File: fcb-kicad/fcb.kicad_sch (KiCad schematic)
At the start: 50 parts, among them J1 Conn_ESC_4in1, J2 SWD, SW1 SW_Push, SW2 SW_SPDT, U1 TPS5430DDA, U2 AMS1117-3.3, U5 STM32F411CEUx, Y1 16 MHz

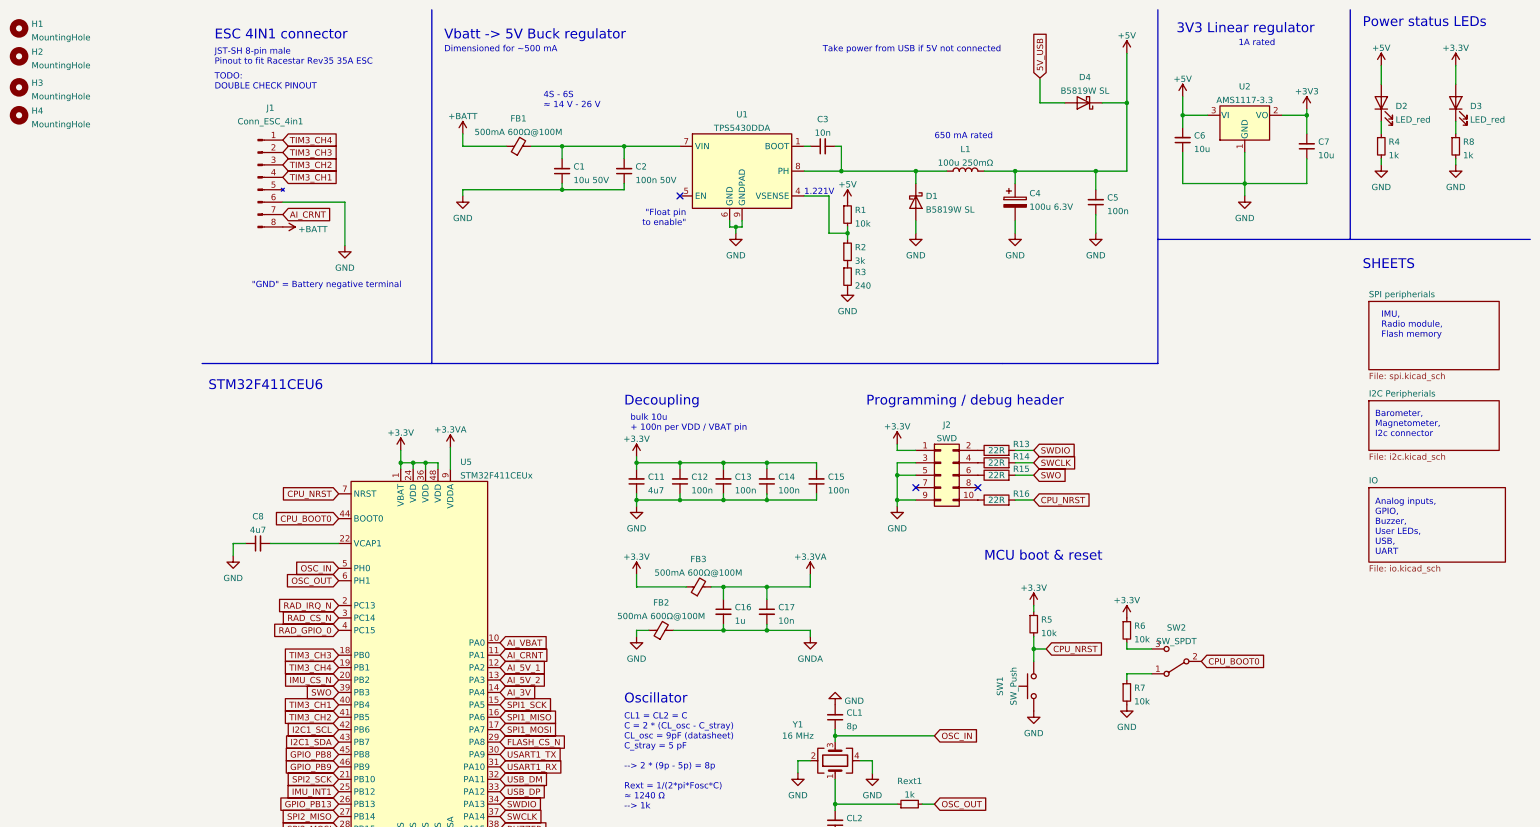
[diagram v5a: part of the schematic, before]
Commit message: buzzer footprint
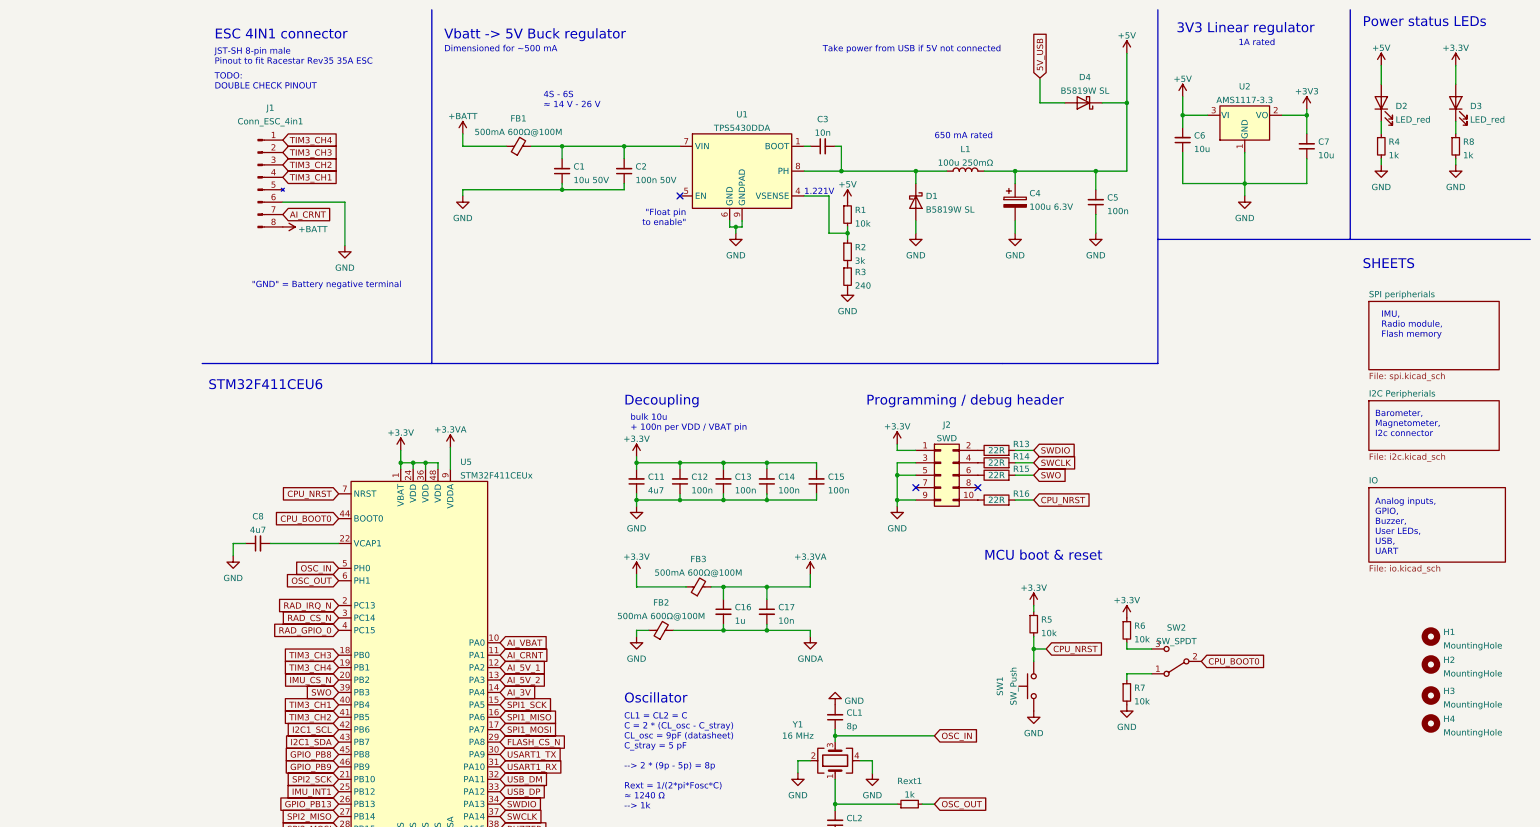
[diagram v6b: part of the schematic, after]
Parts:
- H1, H2, H3, H4: footprint MountingHole:MountingHole_3.2mm_M3 -> MountingHole:MountingHole_3.2mm_M3_DIN965_Pad
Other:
- moved on the sheet: H1, H2, H3, H4
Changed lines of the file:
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@@
     (pin "2")
   )
-  (symbol (lib_id "Mechanical:MountingHole") (at -24.765 34.29 0) (unit 1)
-    (in_bom yes) (on_board yes) (fields_autoplaced)
-    (property "Reference" "H4" (id 0) (at -22.225 33.3815 0)
-      (effects (font (size 1.27 1.27)) (justify left))
-    )
-    (property "Value" "MountingHole" (id 1) (at -22.225 36.1566 0)
-      (effects (font (size 1.27 1.27)) (justify left))
-    )
-    (property "Footprint" "MountingHole:MountingHole_3.2mm_M3" (id 2) (at -24.765 34.29 0)
-      (effects (font (size 1.27 1.27)) hide)
-    )
-    (property "Datasheet" "~" (id 3) (at -24.765 34.29 0)
+  (symbol (lib_id "Mechanical:MountingHole") (at 264.16 158.75 0) (unit 1)
+    (in_bom yes) (on_board yes) (fields_autoplaced)
+    (property "Reference" "H4" (id 0) (at 266.7 157.8415 0)
+      (effects (font (size 1.27 1.27)) (justify left))
+    )
+    (property "Value" "MountingHole" (id 1) (at 266.7 160.6166 0)
+      (effects (font (size 1.27 1.27)) (justify left))
+    )
+    (property "Footprint" "MountingHole:MountingHole_3.2mm_M3_DIN965_Pad" (id 2) (at 264.16 158.75 0)
+      (effects (font (size 1.27 1.27)) hide)
+    )
+    (property "Datasheet" "~" (id 3) (at 264.16 158.75 0)
       (effects (font (size 1.27 1.27)) hide)
     )
@@
     (pin "2")
   )
-  (symbol (lib_id "Mechanical:MountingHole") (at -24.765 16.51 0) (unit 1)
-    (in_bom yes) (on_board yes) (fields_autoplaced)
-    (property "Reference" "H1" (id 0) (at -22.225 15.6015 0)
-      (effects (font (size 1.27 1.27)) (justify left))
-    )
-    (property "Value" "MountingHole" (id 1) (at -22.225 18.3766 0)
-      (effects (font (size 1.27 1.27)) (justify left))
-    )
-    (property "Footprint" "MountingHole:MountingHole_3.2mm_M3" (id 2) (at -24.765 16.51 0)
-      (effects (font (size 1.27 1.27)) hide)
-    )
-    (property "Datasheet" "~" (id 3) (at -24.765 16.51 0)
+  (symbol (lib_id "Mechanical:MountingHole") (at 264.16 140.97 0) (unit 1)
+    (in_bom yes) (on_board yes) (fields_autoplaced)
+    (property "Reference" "H1" (id 0) (at 266.7 140.0615 0)
+      (effects (font (size 1.27 1.27)) (justify left))
+    )
+    (property "Value" "MountingHole" (id 1) (at 266.7 142.8366 0)
+      (effects (font (size 1.27 1.27)) (justify left))
+    )
+    (property "Footprint" "MountingHole:MountingHole_3.2mm_M3_DIN965_Pad" (id 2) (at 264.16 140.97 0)
+      (effects (font (size 1.27 1.27)) hide)
+    )
+    (property "Datasheet" "~" (id 3) (at 264.16 140.97 0)
       (effects (font (size 1.27 1.27)) hide)
     )
@@
     (pin "1")
   )
-  (symbol (lib_id "Mechanical:MountingHole") (at -24.765 28.575 0) (unit 1)
-    (in_bom yes) (on_board yes) (fields_autoplaced)
-    (property "Reference" "H3" (id 0) (at -22.225 27.6665 0)
-      (effects (font (size 1.27 1.27)) (justify left))
-    )
-    (property "Value" "MountingHole" (id 1) (at -22.225 30.4416 0)
-      (effects (font (size 1.27 1.27)) (justify left))
-    )
-    (property "Footprint" "MountingHole:MountingHole_3.2mm_M3" (id 2) (at -24.765 28.575 0)
-      (effects (font (size 1.27 1.27)) hide)
-    )
-    (property "Datasheet" "~" (id 3) (at -24.765 28.575 0)
+  (symbol (lib_id "Mechanical:MountingHole") (at 264.16 153.035 0) (unit 1)
+    (in_bom yes) (on_board yes) (fields_autoplaced)
+    (property "Reference" "H3" (id 0) (at 266.7 152.1265 0)
+      (effects (font (size 1.27 1.27)) (justify left))
+    )
+    (property "Value" "MountingHole" (id 1) (at 266.7 154.9016 0)
+      (effects (font (size 1.27 1.27)) (justify left))
+    )
+    (property "Footprint" "MountingHole:MountingHole_3.2mm_M3_DIN965_Pad" (id 2) (at 264.16 153.035 0)
+      (effects (font (size 1.27 1.27)) hide)
+    )
+    (property "Datasheet" "~" (id 3) (at 264.16 153.035 0)
       (effects (font (size 1.27 1.27)) hide)
     )
@@
     (pin "1")
   )
-  (symbol (lib_id "Mechanical:MountingHole") (at -24.765 22.225 0) (unit 1)
-    (in_bom yes) (on_board yes) (fields_autoplaced)
-    (property "Reference" "H2" (id 0) (at -22.225 21.3165 0)
-      (effects (font (size 1.27 1.27)) (justify left))
-    )
-    (property "Value" "MountingHole" (id 1) (at -22.225 24.0916 0)
-      (effects (font (size 1.27 1.27)) (justify left))
-    )
-    (property "Footprint" "MountingHole:MountingHole_3.2mm_M3" (id 2) (at -24.765 22.225 0)
-      (effects (font (size 1.27 1.27)) hide)
-    )
-    (property "Datasheet" "~" (id 3) (at -24.765 22.225 0)
+  (symbol (lib_id "Mechanical:MountingHole") (at 264.16 146.685 0) (unit 1)
+    (in_bom yes) (on_board yes) (fields_autoplaced)
+    (property "Reference" "H2" (id 0) (at 266.7 145.7765 0)
+      (effects (font (size 1.27 1.27)) (justify left))
+    )
+    (property "Value" "MountingHole" (id 1) (at 266.7 148.5516 0)
+      (effects (font (size 1.27 1.27)) (justify left))
+    )
+    (property "Footprint" "MountingHole:MountingHole_3.2mm_M3_DIN965_Pad" (id 2) (at 264.16 146.685 0)
+      (effects (font (size 1.27 1.27)) hide)
+    )
+    (property "Datasheet" "~" (id 3) (at 264.16 146.685 0)
       (effects (font (size 1.27 1.27)) hide)
     )
@@
     )
     (path "/5a53718f-be21-42e3-8a71-3f39996f502c/d95f445b-a344-4489-9ecd-212419bfd59e"
-      (reference "BZ1") (unit 1) (value "MLT-8530") (footprint "Buzzer_Beeper:Buzzer_TDK_PS1240P02BT_D12.2mm_H6.5mm")
+      (reference "BZ1") (unit 1) (value "MLT-8530") (footprint "000_sjt:MLT-8350")
     )
     (path "/e73a660a-d13e-45db-86a7-32a58cc13355"
@@
     )
     (path "/4b64061a-4166-4c51-afb2-f57d202f9649"
-      (reference "H1") (unit 1) (value "MountingHole") (footprint "MountingHole:MountingHole_3.2mm_M3")
+      (reference "H1") (unit 1) (value "MountingHole") (footprint "MountingHole:MountingHole_3.2mm_M3_DIN965_Pad")
     )
     (path "/ce82bad6-71aa-4e24-b36b-840272b7c2a8"
-      (reference "H2") (unit 1) (value "MountingHole") (footprint "MountingHole:MountingHole_3.2mm_M3")
+      (reference "H2") (unit 1) (value "MountingHole") (footprint "MountingHole:MountingHole_3.2mm_M3_DIN965_Pad")
     )
     (path "/8c8730ef-8afc-440c-bb89-45bbd19f3ef4"
-      (reference "H3") (unit 1) (value "MountingHole") (footprint "MountingHole:MountingHole_3.2mm_M3")
+      (reference "H3") (unit 1) (value "MountingHole") (footprint "MountingHole:MountingHole_3.2mm_M3_DIN965_Pad")
     )
     (path "/430209ac-5306-4944-be0d-ad99694bc4d6"
-      (reference "H4") (unit 1) (value "MountingHole") (footprint "MountingHole:MountingHole_3.2mm_M3")
+      (reference "H4") (unit 1) (value "MountingHole") (footprint "MountingHole:MountingHole_3.2mm_M3_DIN965_Pad")
     )
     (path "/3ba9f5ad-34c6-4809-aca1-124bdec46130"

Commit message: buzzer notes
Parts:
- Y1: footprint (none) -> Crystal:Crystal_SMD_3225-4Pin_3.2x2.5mm
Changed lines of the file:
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@@
     (property "Reference" "Y1" (id 0) (at 134.62 158.9851 90))
     (property "Value" "16 MHz" (id 1) (at 134.62 161.29 90))
-    (property "Footprint" "" (id 2) (at 142.24 166.37 0)
-      (effects (font (size 1.27 1.27)) hide)
-    )
-    (property "Datasheet" "~" (id 3) (at 142.24 166.37 0)
+    (property "Footprint" "Crystal:Crystal_SMD_3225-4Pin_3.2x2.5mm" (id 2) (at 142.24 166.37 0)
+      (effects (font (size 1.27 1.27)) hide)
+    )
+    (property "Datasheet" "https://datasheet.lcsc.com/lcsc/2103291133_Yangxing-Tech-X322516MLB4SI_C13738.pdf" (id 3) (at 142.24 166.37 0)
       (effects (font (size 1.27 1.27)) hide)
     )
@@
       (reference "#PWR035") (unit 1) (value "GND") (footprint "")
     )
-    (path "/5a53718f-be21-42e3-8a71-3f39996f502c/21d68f7c-e448-4eec-ba4b-b89693d2d5ab"
-      (reference "#PWR036") (unit 1) (value "+5V") (footprint "")
-    )
     (path "/5a53718f-be21-42e3-8a71-3f39996f502c/8edebb43-249a-4e9c-bf35-8120dc9fece3"
       (reference "#PWR037") (unit 1) (value "GND") (footprint "")
@@
       (reference "#PWR0120") (unit 1) (value "+3V3") (footprint "")
     )
+    (path "/5a53718f-be21-42e3-8a71-3f39996f502c/40036466-b8fa-436d-bfc3-d3e3c4c64291"
+      (reference "#PWR?") (unit 1) (value "+3V3") (footprint "")
+    )
     (path "/5a53718f-be21-42e3-8a71-3f39996f502c/d95f445b-a344-4489-9ecd-212419bfd59e"
       (reference "BZ1") (unit 1) (value "MLT-8530") (footprint "000_sjt:MLT-8350")
@@
     )
     (path "/a04f48b5-074d-4b8b-a90e-d46d3e6098cc"
-      (reference "Y1") (unit 1) (value "16 MHz") (footprint "")
-    )
-  )
+      (reference "Y1") (unit 1) (value "16 MHz") (footprint "Crystal:Crystal_SMD_3225-4Pin_3.2x2.5mm")
+    )
+  )
